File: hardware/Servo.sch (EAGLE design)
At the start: 13 parts, among them Q1 AOD417, U1 PCA9685

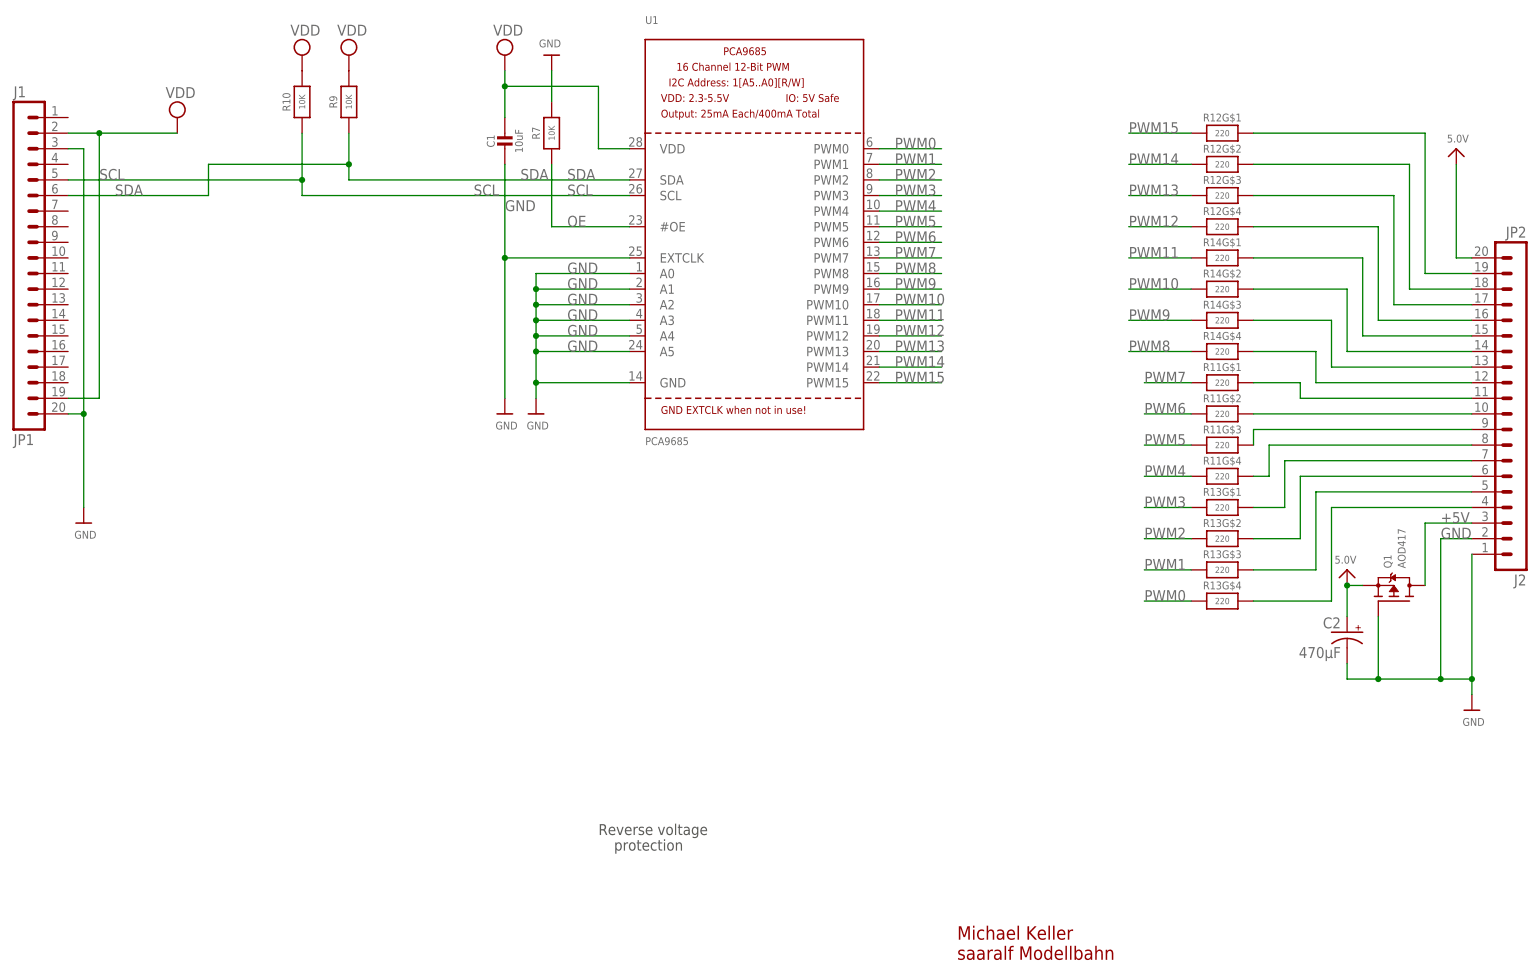
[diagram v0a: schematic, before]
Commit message: Wiederstände als 0803
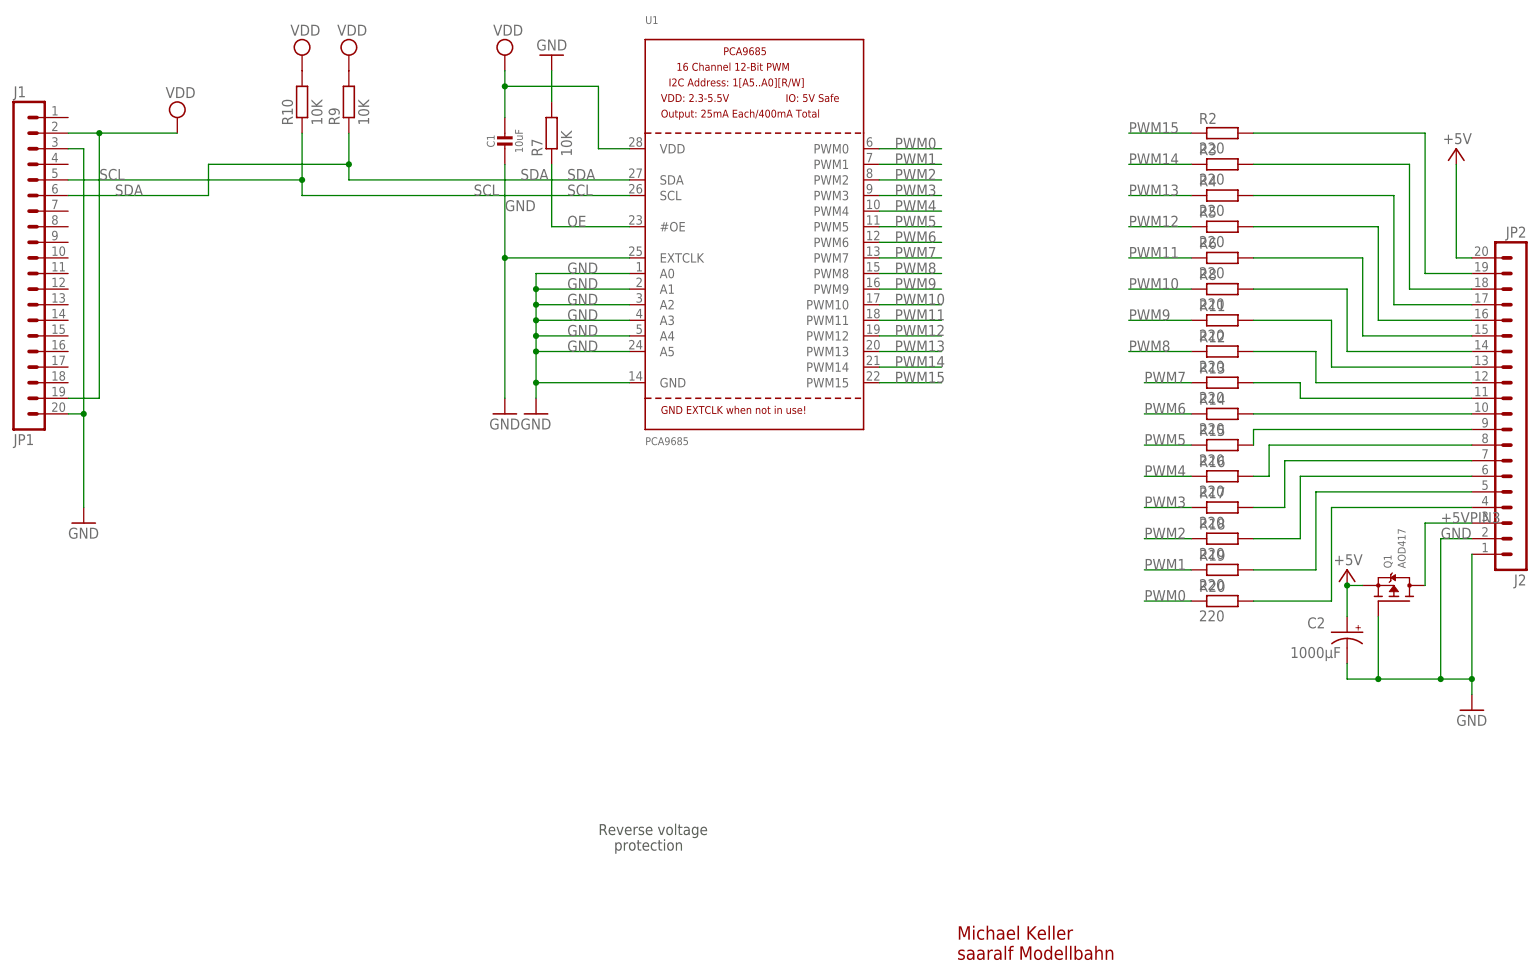
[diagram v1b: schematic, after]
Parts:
- added R15, R16, R17, R18, R19, R2, R20, R3, R4, R5, R6, R8: 220, rcl:R-EU_M0805
- C2: value 470µF -> 1000µF
- R10, R7, R9: device microbuilder:RESISTOR0805_NOOUTLINE -> rcl:R-EU_M0805
- R11, R12, R13, R14: device microbuilder:RESISTOR_4PACK -> rcl:R-EU_M0805
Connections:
- removed net 5.0V: C2.+, JP2.20, Q1.S
- new net +5VPIN3: JP2.3, Q1.D
- net +5V: now also C2.+, JP2.20, Q1.S; no longer JP2.3, Q1.D
- net N$10: now also R6.2; no longer R14G$1.2
- net N$11: now also R8.2; no longer R14G$2.2
- net N$12: now also R3.2; no longer R12G$2.2
- net N$13: now also R11.2; no longer R14G$3.2
- net N$14: now also R2.2; no longer R12G$1.2
- net N$15: now also R16.2; no longer R11G$4.2
- net N$17: now also R5.2; no longer R12G$4.2
- net N$18: now also R12.2; no longer R14G$4.2
- net N$2: now also R4.2; no longer R12G$3.2
- net N$3: now also R13.2; no longer R11G$1.2
- net N$4: now also R14.2; no longer R11G$2.2
- net N$5: now also R15.2; no longer R11G$3.2
- net N$6: now also R17.2; no longer R13G$1.2
- net N$7: now also R18.2; no longer R13G$2.2
- net N$8: now also R19.2; no longer R13G$3.2
- net N$9: now also R20.2; no longer R13G$4.2
- net PWM0: now also R20.1; no longer R13G$4.1
- net PWM1: now also R19.1; no longer R13G$3.1
- net PWM10: now also R8.1; no longer R14G$2.1
- net PWM11: now also R6.1; no longer R14G$1.1
- net PWM12: now also R5.1; no longer R12G$4.1
- net PWM13: now also R4.1; no longer R12G$3.1
- net PWM14: now also R3.1; no longer R12G$2.1
- net PWM15: now also R2.1; no longer R12G$1.1
- net PWM2: now also R18.1; no longer R13G$2.1
- net PWM3: now also R17.1; no longer R13G$1.1
- net PWM4: now also R16.1; no longer R11G$4.1
- net PWM5: now also R15.1; no longer R11G$3.1
- net PWM6: now also R14.1; no longer R11G$2.1
- net PWM7: now also R13.1; no longer R11G$1.1
- net PWM8: now also R12.1; no longer R14G$4.1
- net PWM9: now also R11.1; no longer R14G$3.1
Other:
- moved on the sheet: R11, R12, R13, R14

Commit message: Neue Version V2 des ServoAufsatzes
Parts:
- removed Q1: AOD417, microbuilder:MOSFET-PTO252
- added Q2: IRLML6401, microbuilder:MOSFET-PWIDE
- renumbered U1 to PCA9685
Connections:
- net +5V: now also Q2.S; no longer Q1.S
- net +5VPIN3: now also Q2.D; no longer Q1.D
- net GND: now also Q2.G; no longer Q1.G
